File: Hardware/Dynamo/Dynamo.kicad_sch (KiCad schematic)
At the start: 44 parts, among them U1 AP63205WU, U10 ESP32-S3-WROOM-1, U11 NCP1117-3.3_SOT223, U13 TXS0102DCT, U14 TXS0102DCT, U2 TLP2770, U3 TLP2770, U4 74LVC1G86, U5 74LVC1G86, U6 74LVC1G86, U7 74LVC1G86, U8 74LVC1G86, U9 74LVC1G86

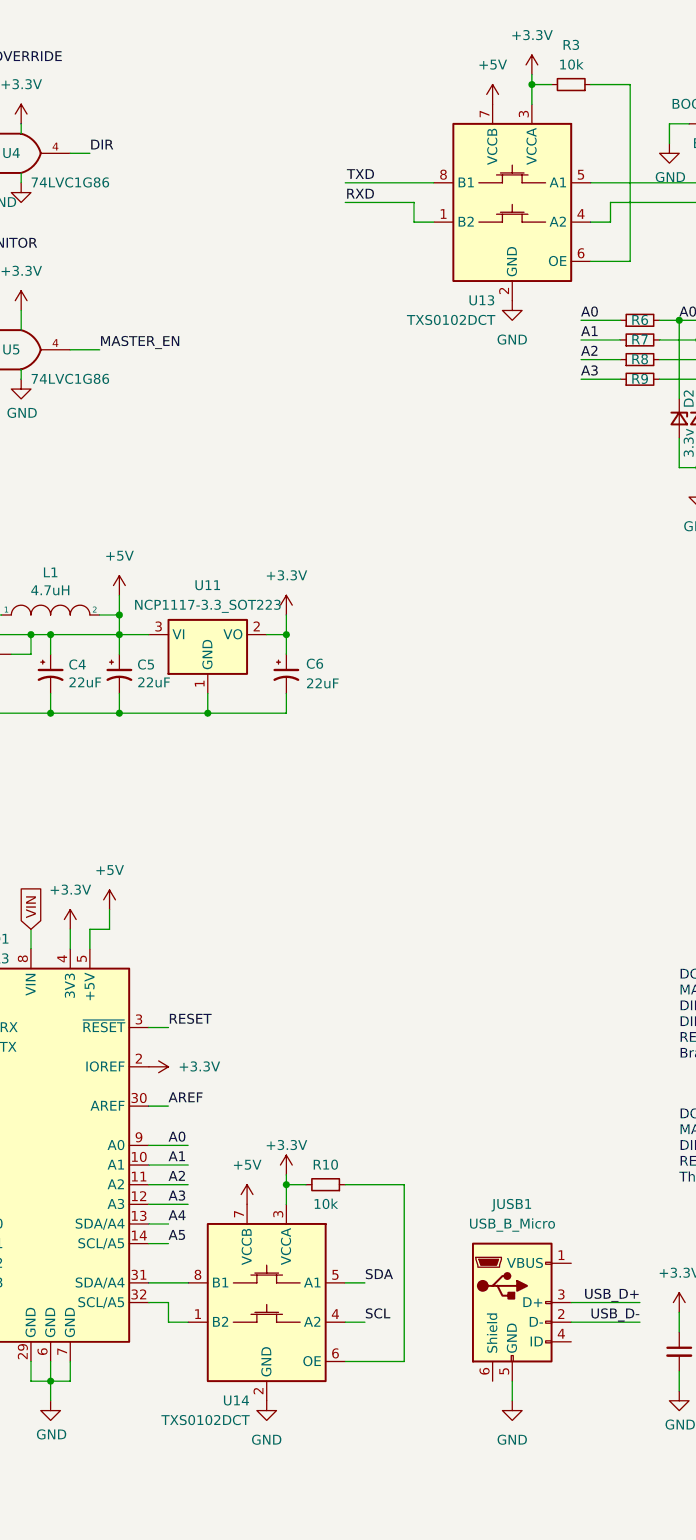
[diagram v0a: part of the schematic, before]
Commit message: Completed BOM, minor changes to schematic and PCB
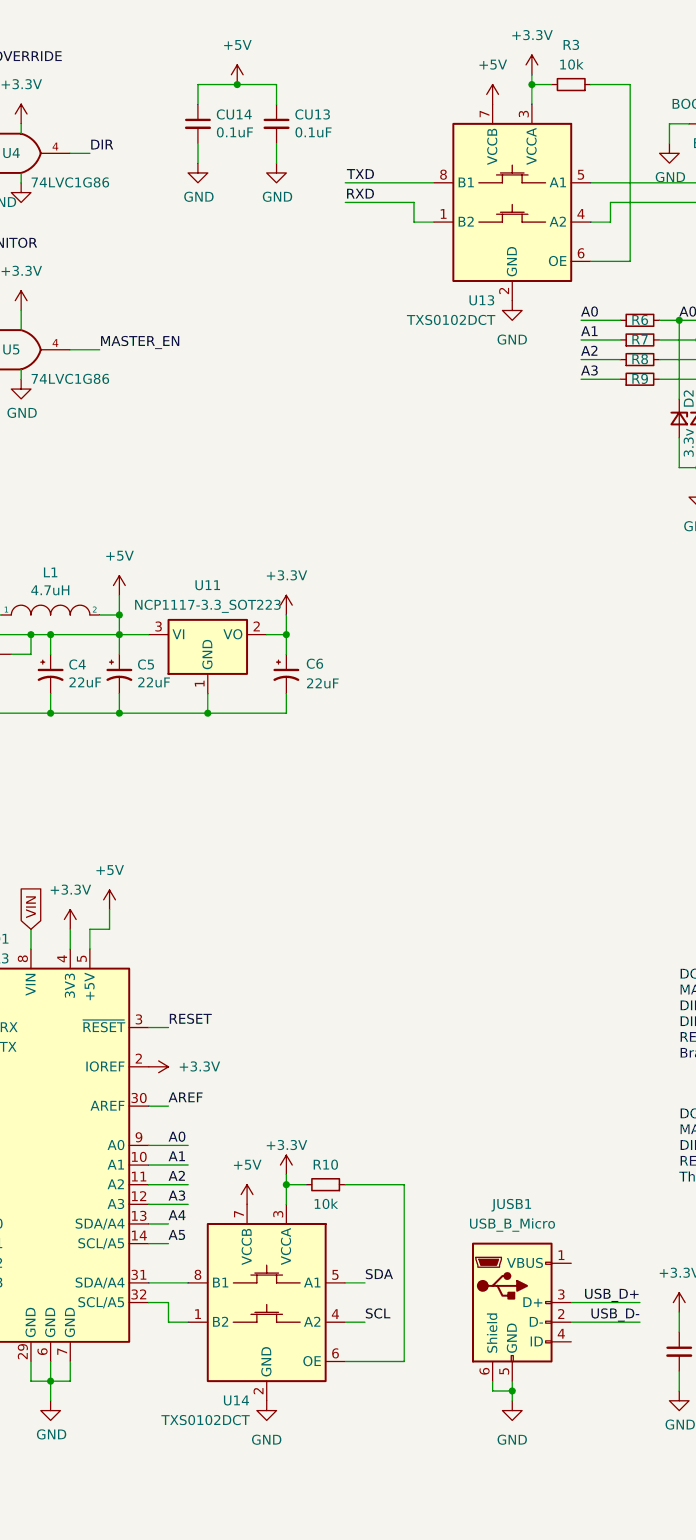
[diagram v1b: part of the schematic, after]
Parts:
- added CU13, CU14: 0.1uF, Capacitor_SMD:C_1206_3216Metric, symbol Device:C_Small
- D1: MFG (none) -> Wurth Elektronik
- D2, D3, D4, D5: footprint Diode_SMD:D_1206_3216Metric -> Diode_SMD:D_SOD-123; MFG (none) -> Diodes Incorporated; PN (none) -> BZT52C3V3-7-F
- R1: MFG Bourns -> YAEGO; PN CR1206-FX-3001ELF -> RC1206FR-073KL
- R10, R3, R4, R5: MFG Bourns -> YAEGO; PN CR1206-FX-1002ELF -> RC1206FR-1310KL
- R2: MFG Bourns -> YAEGO; PN CR1206-FX-1001ELF -> RC1206FR-071KL
- R6, R7, R8, R9: MFG (none) -> YAEGO; PN (none) -> RC1206FR-071KL
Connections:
- net +5V: now also CU13.1, CU14.1
- net GND: now also JUSB1.6 (Shield), CU13.2, CU14.2

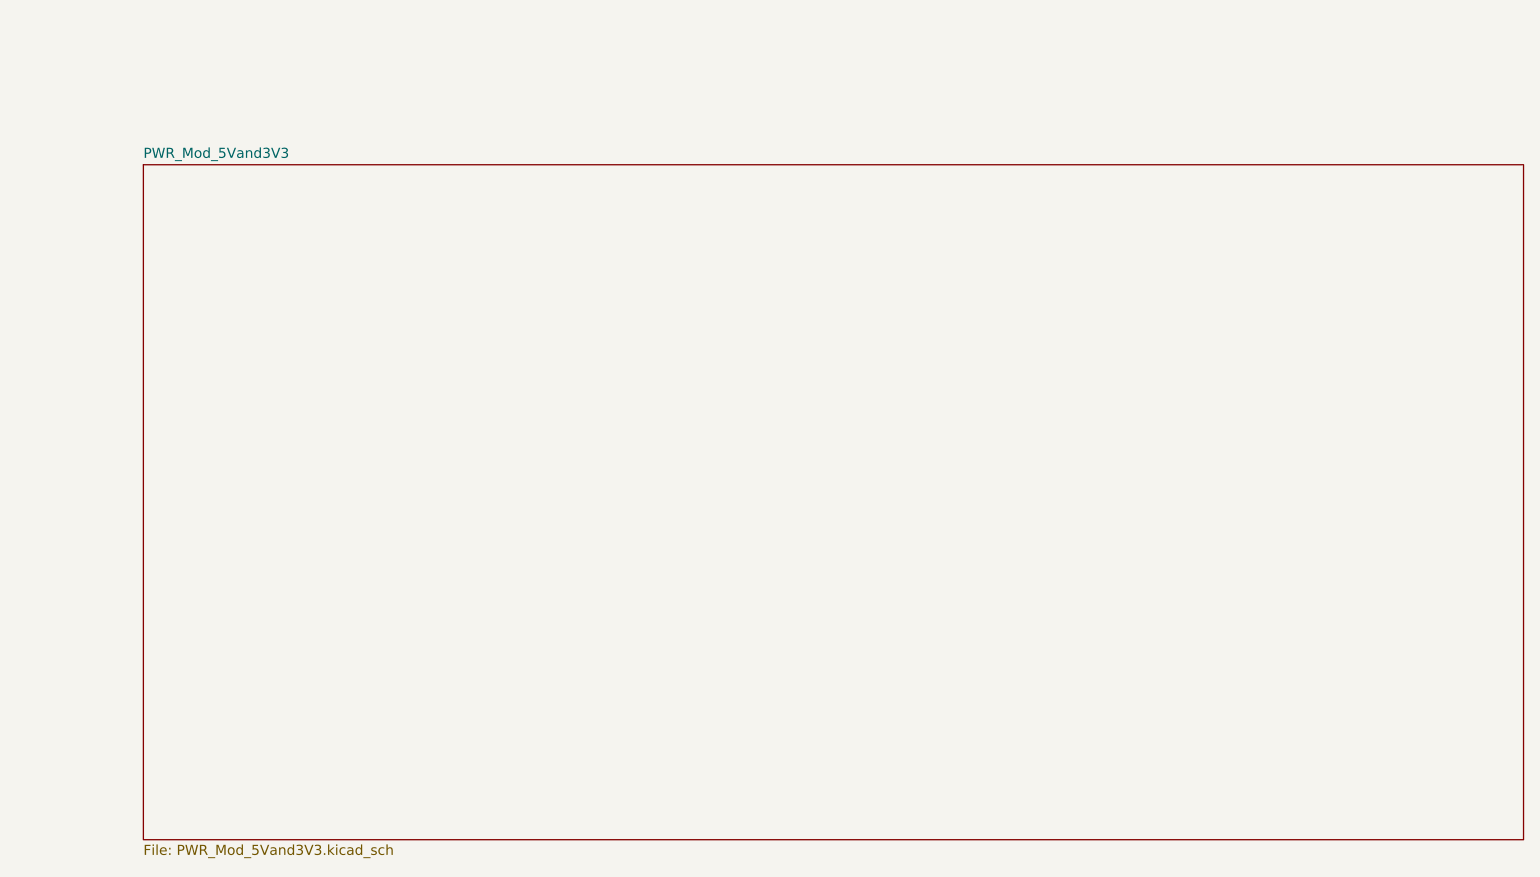
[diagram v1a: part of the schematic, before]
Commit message: Fixed i2c_init, added rmt_rx_init and rmt_tx_init. Consider making a class arch( to hold all this HAL stuff
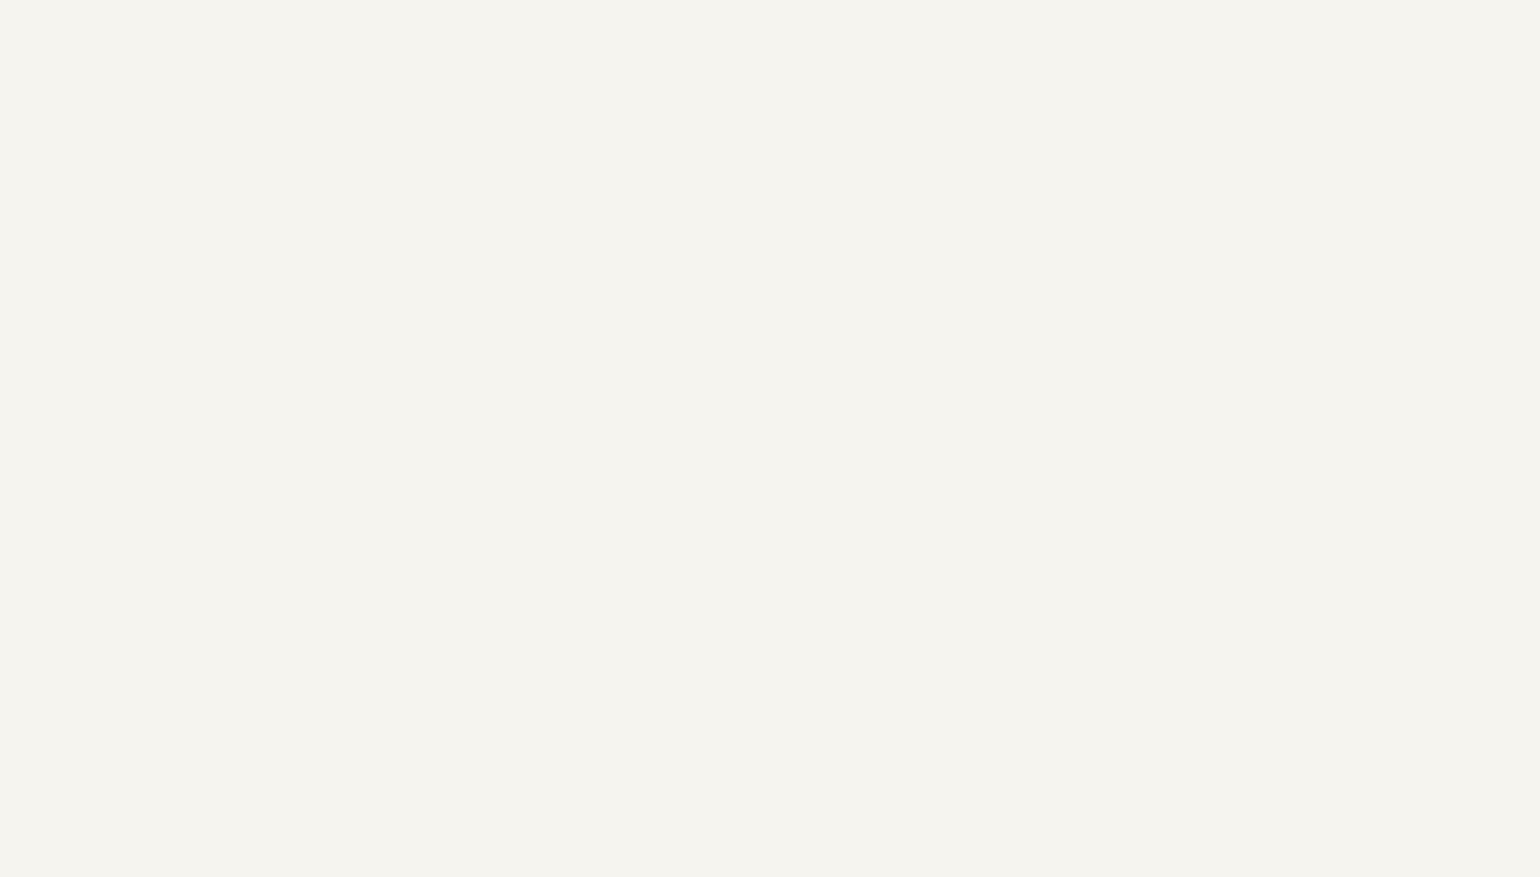
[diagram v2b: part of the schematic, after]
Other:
- removed sheet PWR_Mod_5Vand3V3
- company: (none) -> SeraphimLabs LLC
- title: (none) -> Dynamo - DCC 4 channel booster
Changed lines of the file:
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@@
 (kicad_sch (version 20230121) (generator eeschema)
   (paper "A4")
+  (title_block
+    (title "Dynamo - DCC 4 channel booster")
+    (company "SeraphimLabs LLC")
+  )
   (junction (at 38.1 101.6) (diameter 0) (color 0 0 0 0)
   )
@@
           (reference "C6") (unit 1)
         )
-        (path "/ca466827-dc9b-41a9-af5b-af8cb0cad0b9/9cefd538-1e06-4e68-b561-c42257c55829"
-          (reference "C11") (unit 1)
-        )
       )
     )
@@
           (reference "C5") (unit 1)
         )
-        (path "/ca466827-dc9b-41a9-af5b-af8cb0cad0b9/9cefd538-1e06-4e68-b561-c42257c55829"
-          (reference "C5") (unit 1)
-        )
       )
     )
@@
           (reference "D1") (unit 1)
         )
-        (path "/ca466827-dc9b-41a9-af5b-af8cb0cad0b9/9cefd538-1e06-4e68-b561-c42257c55829"
-          (reference "D2") (unit 1)
-        )
       )
     )
@@
           (reference "U1") (unit 1)
         )
-        (path "/ca466827-dc9b-41a9-af5b-af8cb0cad0b9/9cefd538-1e06-4e68-b561-c42257c55829"
-          (reference "U1") (unit 1)
-        )
       )
     )
@@
           (reference "C2") (unit 1)
         )
-        (path "/ca466827-dc9b-41a9-af5b-af8cb0cad0b9/9cefd538-1e06-4e68-b561-c42257c55829"
-          (reference "C2") (unit 1)
-        )
       )
     )
@@
           (reference "R2") (unit 1)
         )
-        (path "/ca466827-dc9b-41a9-af5b-af8cb0cad0b9/9cefd538-1e06-4e68-b561-c42257c55829"
-          (reference "R2") (unit 1)
-        )
       )
     )
@@
           (reference "#PWR013") (unit 1)
         )
-        (path "/ca466827-dc9b-41a9-af5b-af8cb0cad0b9/9cefd538-1e06-4e68-b561-c42257c55829"
-          (reference "#PWR013") (unit 1)
-        )
       )
     )
@@
           (reference "C3") (unit 1)
         )
-        (path "/ca466827-dc9b-41a9-af5b-af8cb0cad0b9/9cefd538-1e06-4e68-b561-c42257c55829"
-          (reference "C3") (unit 1)
-        )
       )
     )
@@
           (reference "C4") (unit 1)
         )
-        (path "/ca466827-dc9b-41a9-af5b-af8cb0cad0b9/9cefd538-1e06-4e68-b561-c42257c55829"
-          (reference "C4") (unit 1)
-        )
       )
     )
@@
           (reference "L1") (unit 1)
         )
-        (path "/ca466827-dc9b-41a9-af5b-af8cb0cad0b9/9cefd538-1e06-4e68-b561-c42257c55829"
-          (reference "L2") (unit 1)
-        )
       )
     )
@@
       )
     )
-  )
-  (sheet (at 213.36 271.78) (size 173.99 85.09) (fields_autoplaced)
-    (stroke (width 0.1524) (type solid))
-    (fill (color 0 0 0 0.0000))
-    (property "Sheetname" "PWR_Mod_5Vand3V3" (at 213.36 271.0684 0)
-      (effects (font (size 1.27 1.27)) (justify left bottom))
-    )
-    (property "Sheetfile" "PWR_Mod_5Vand3V3.kicad_sch" (at 213.36 357.4546 0)
-      (effects (font (size 1.27 1.27)) (justify left top))
-    )
-    (instances
-      (project "Dynamo"
-        (path "/ca466827-dc9b-41a9-af5b-af8cb0cad0b9" (page "2"))
-      )
-    )

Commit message: Revised L1 for possible 2A output, cleaner fill zones, fabrication outputs
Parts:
- L1: footprint Inductor_SMD:L_1008_2520Metric_Pad1.43x2.20mm_HandSolder -> Inductor_SMD_Wurth:L_Wurth_WE-LQSH-4020; MFG Murata Electronics -> Wuerth Electronik; PN LQM2HPN4R7MGCL -> 74405042047
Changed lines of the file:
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@@
       (effects (font (size 1.27 1.27)))
     )
-    (property "Footprint" "Inductor_SMD:L_1008_2520Metric_Pad1.43x2.20mm_HandSolder" (at 67.31 88.9 0)
+    (property "Footprint" "Inductor_SMD_Wurth:L_Wurth_WE-LQSH-4020" (at 67.31 88.9 0)
       (effects (font (size 1.27 1.27)) hide)
     )
-    (property "Datasheet" "https://www.mouser.com/datasheet/2/281/1/JELF243B_0025-1634213.pdf" (at 67.31 88.9 0)
+    (property "Datasheet" "https://www.mouser.com/datasheet/2/281/JELF243A-0147-1699525.pdf" (at 67.31 88.9 0)
       (effects (font (size 1.27 1.27)) hide)
     )
-    (property "MFG" "Murata Electronics" (at 67.31 88.9 0)
+    (property "MFG" "Wuerth Electronik" (at 67.31 88.9 0)
       (effects (font (size 1.27 1.27)) hide)
     )
-    (property "PN" "LQM2HPN4R7MGCL " (at 67.31 88.9 0)
+    (property "PN" "74405042047" (at 67.31 88.9 0)
       (effects (font (size 1.27 1.27)) hide)
     )

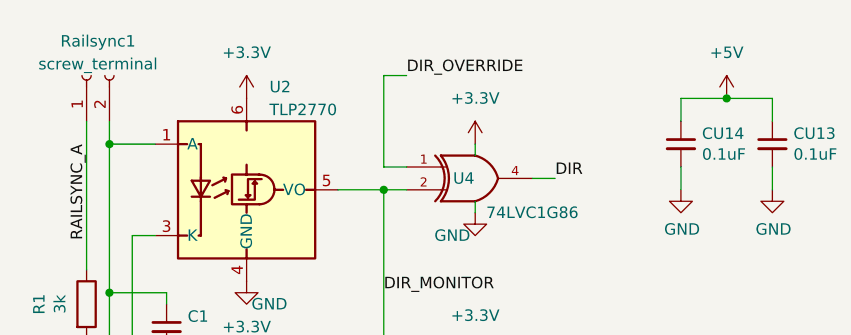
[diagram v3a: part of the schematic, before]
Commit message: Added note about railsync terminal plug, BOM cleanup.
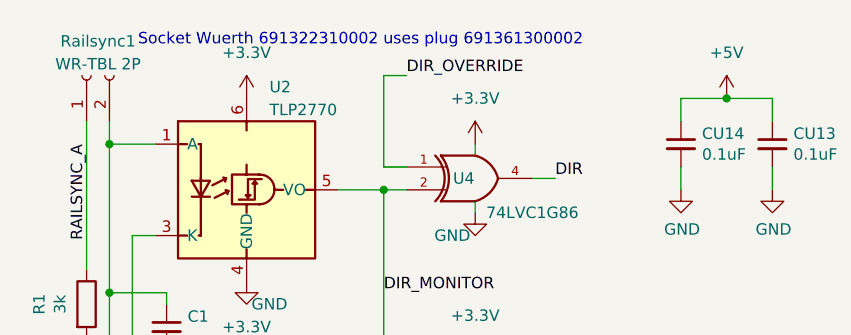
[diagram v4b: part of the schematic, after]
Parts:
- Railsync1: value screw_terminal -> WR-TBL 2P
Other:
- note added: "Socket Wuerth 691322310002 uses plug 691361300002"
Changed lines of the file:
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@@
+    (effects (font (size 1.27 1.27)) (justify left bottom))
+  )
+  (text "Socket Wuerth 691322310002 uses plug 691361300002" (at 26.035 14.605 0)
     (effects (font (size 1.27 1.27)) (justify left bottom))
   )
@@
       (effects (font (size 1.27 1.27)))
     )
-    (property "Value" "screw_terminal" (at 21.59 16.51 90)
+    (property "Value" "WR-TBL 2P" (at 21.59 16.51 90)
       (effects (font (size 1.27 1.27)))
     )
@@
       (effects (font (size 1.27 1.27)) hide)
     )
-    (property "Datasheet" "https://www.mouser.com/datasheet/2/54/cr-1858361.pdf" (at 261.62 25.4 0)
+    (property "Datasheet" "~" (at 261.62 25.4 0)
       (effects (font (size 1.27 1.27)) hide)
     )
@@
       (effects (font (size 1.27 1.27)) hide)
     )
-    (property "Datasheet" "https://www.mouser.com/datasheet/2/54/cr-1858361.pdf" (at 134.62 20.32 0)
+    (property "Datasheet" "~" (at 134.62 20.32 0)
       (effects (font (size 1.27 1.27)) hide)
     )
@@
       (effects (font (size 1.27 1.27)) hide)
     )
-    (property "Datasheet" "https://www.mouser.com/datasheet/2/54/cr-1858361.pdf" (at 170.18 25.4 0)
+    (property "Datasheet" "~" (at 170.18 25.4 0)
       (effects (font (size 1.27 1.27)) hide)
     )
@@
       (effects (font (size 1.27 1.27)) hide)
     )
-    (property "Datasheet" "https://www.mouser.com/datasheet/2/54/cr-1858361.pdf" (at 102.87 162.56 0)
-      (effects (font (size 1.27 1.27)) hide)
-    )
+    (property "Datasheet" "~" (at 102.87 162.56 0)
+      (effects (font (size 1.27 1.27)) hide)
+    )

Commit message: TrackChannel struct + extern in main working, MAX_TRACKS not accessible in main
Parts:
- U10: footprint RF_Module:ESP32-S3-WROOM-1U -> Espressif:ESP32-S3-WROOM-1U
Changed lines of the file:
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@@
       (effects (font (size 1.27 1.27)) (justify left))
     )
-    (property "Footprint" "RF_Module:ESP32-S3-WROOM-1U" (at 215.9 116.84 0)
+    (property "Footprint" "Espressif:ESP32-S3-WROOM-1U" (at 215.9 116.84 0)
       (effects (font (size 1.27 1.27)) hide)
     )
